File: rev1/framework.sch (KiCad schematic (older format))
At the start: 142 parts, among them J1 AVR-ISP-6, J2 USB_C_Receptacle_USB2.0, SW1 SW_Push, SW10 SW_Push_45deg, SW11 SW_Push_45deg, SW12 SW_Push_45deg, SW13 SW_Push_45deg, SW14 SW_Push_45deg, SW15 SW_Push_45deg, SW16 SW_Push_45deg, SW17 SW_Push_45deg, SW18 SW_Push_45deg, SW19 SW_Push_45deg, SW2 SW_Push, SW20 SW_Push_45deg, SW21 SW_Push_45deg, SW22 SW_Push_45deg, SW23 SW_Push_45deg, SW24 SW_Push_45deg, SW25 SW_Push_45deg, SW26 SW_Push_45deg, SW27 SW_Push_45deg, SW28 SW_Push_45deg, SW29 SW_Push_45deg, SW3 SW_Push_45deg, SW30 SW_Push_45deg, SW31 SW_Push_45deg, SW32 SW_Push_45deg, SW33 SW_Push_45deg, SW34 SW_Push_45deg, SW35 SW_Push_45deg, SW36 SW_Push_45deg, SW37 SW_Push_45deg, SW38 SW_Push_45deg, SW39 SW_Push_45deg, SW4 SW_Push_45deg, SW40 SW_Push_45deg, SW41 SW_Push_45deg, SW42 SW_Push_45deg, SW43 SW_Push_45deg, SW44 SW_Push_45deg, SW45 SW_Push_45deg, SW46 SW_Push_45deg, SW47 SW_Push_45deg, SW48 SW_Push_45deg, SW49 SW_Push_45deg, SW5 SW_Push_45deg, SW50 SW_Push_45deg, SW51 SW_Push_45deg, SW52 SW_Push_45deg, SW53 SW_Push_45deg, SW54 SW_Push_45deg, SW55 SW_Push_45deg, SW56 SW_Push_45deg, SW57 SW_Push_45deg, SW58 SW_Push_45deg, SW59 SW_Push_45deg, SW6 SW_Push_45deg, SW60 SW_Push_45deg, SW61 SW_Push_45deg, SW62 SW_Push_45deg, SW63 Rotary_Encoder_Switch, SW64 SW_Push_45deg, SW65 SW_Push_45deg, SW7 SW_Push_45deg, SW8 SW_Push_45deg, SW9 SW_Push_45deg, U1 ATmega328P-PU, Y1 16M

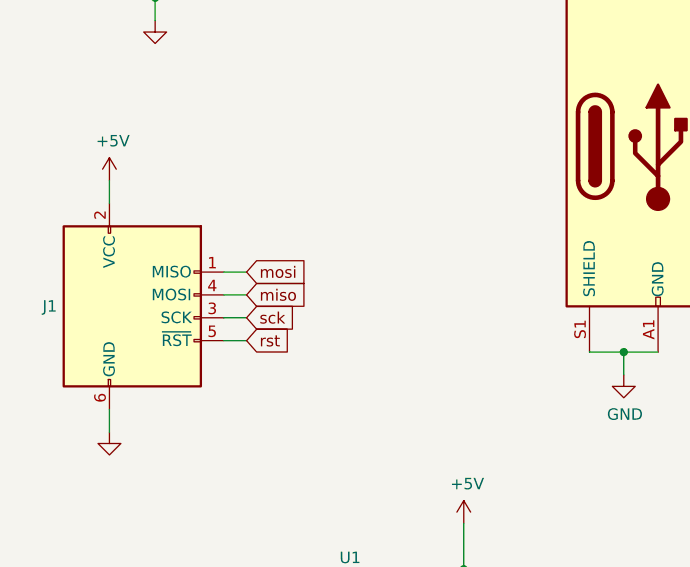
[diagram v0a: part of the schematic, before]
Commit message: Fix mixed up MOSI and MISO connections for ISP
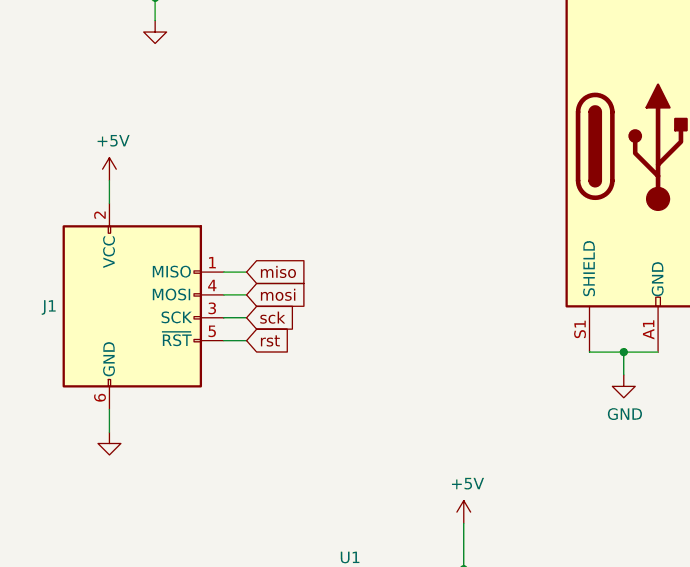
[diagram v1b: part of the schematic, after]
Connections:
- net miso: now also J1.1 (MISO); no longer J1.4 (MOSI)
- net mosi: now also J1.4 (MOSI); no longer J1.1 (MISO)
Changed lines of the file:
@@
 Wire Wire Line
 	3650 5650 3700 5650
+Text GLabel 2100 2550 2    50   Input ~ 0
+miso
 Text GLabel 2100 2650 2    50   Input ~ 0
-miso
-Text GLabel 2100 2550 2    50   Input ~ 0
 mosi
 Text GLabel 2100 2750 2    50   Input ~ 0

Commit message: correct schematic: schottky to zener diode symbols on USB d+/d-
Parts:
- D1, D2: symbol Device:D_Schottky_Small -> Device:D_Zener_Small
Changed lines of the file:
@@
 $EndComp
 $Comp
-L Device:D_Schottky_Small D1
-U 1 1 5FDB4278
-P 4600 2800
-F 0 "D1" V 4554 2868 50  0000 L CNN
-F 1 "3v6" V 4645 2868 50  0000 L CNN
-F 2 "framework:D_DO-35_SOD27_P7.62mm_Horizontal" V 4600 2800 50  0001 C CNN
-F 3 "~" V 4600 2800 50  0001 C CNN
-F 4 "https://www.digikey.ca/en/products/detail/on-semiconductor/BZX79C3V6/977916" V 4600 2800 50  0001 C CNN "DigiKey"
-	1    4600 2800
-	0    1    1    0
-$EndComp
-$Comp
-L Device:D_Schottky_Small D2
+L Device:D_Zener_Small D2
 U 1 1 5FDB427F
 P 4900 2800
@@
 	6700 5400 7400 5400
 Connection ~ 7400 5400
+$Comp
+L Device:D_Zener_Small D1
+U 1 1 5FDB4278
+P 4600 2800
+F 0 "D1" V 4554 2868 50  0000 L CNN
+F 1 "3v6" V 4645 2868 50  0000 L CNN
+F 2 "framework:D_DO-35_SOD27_P7.62mm_Horizontal" V 4600 2800 50  0001 C CNN
+F 3 "~" V 4600 2800 50  0001 C CNN
+F 4 "https://www.digikey.ca/en/products/detail/on-semiconductor/BZX79C3V6/977916" V 4600 2800 50  0001 C CNN "DigiKey"
+	1    4600 2800
+	0    1    1    0
+$EndComp
 $EndSCHEMATC
